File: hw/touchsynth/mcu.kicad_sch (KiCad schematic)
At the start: 10 parts, among them J2 SWIO, J3 MIDI IN, U3 CH32V003F4P6 / CH32V002F4P6, U4 LTV-817S

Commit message: Schematic v2: hand-drawn sheet layouts with wires; MIDI in DNP
- draw.py/gen_sch2.py/layouts.py: placement + wiring per block, automatic
  labels for remaining split nets, short detection, junctions, KiCad
  endpoint-only connection semantics
- all 7 sheets laid out (ladder drawn as a transistor stack, diff amps,
  integrator with reset, R-2R DAC, ...); ERC 0 violations, netlist == design,
  145 simulated elements match
- MIDI input parts marked DNP (footprints kept)
- docs/touchsynth_schematic.pdf

Co-Authored-By: Claude Opus 5.5 (1M context) <noreply@anthropic.com>
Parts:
- D2, R14, R15, U4: now not fitted
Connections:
- net MIDI_4: no longer names the net of J3.1 (Pin_1), R14.1
- net MIDI_5: no longer names the net of D2.2 (A), J3.2 (Pin_2), U4.2
- net MIDI_A: no longer names the net of D2.1 (K), R14.2, U4.1
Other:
- note added: "MCU: CH32V003F4P6 or CH32V002F4P6 (TSSOP-20, hand-soldered, not placed by JLCPCB)"
- note added: "MIDI in (not populated in rev 0.1)"
- note added: "Programming (WCH-LinkE, SWIO)"
- note removed: "MCU (CH32V003 / CH32V002, hand-soldered)"
- note removed: "MIDI in"
- note removed: "Programming (WCH-LinkE)"

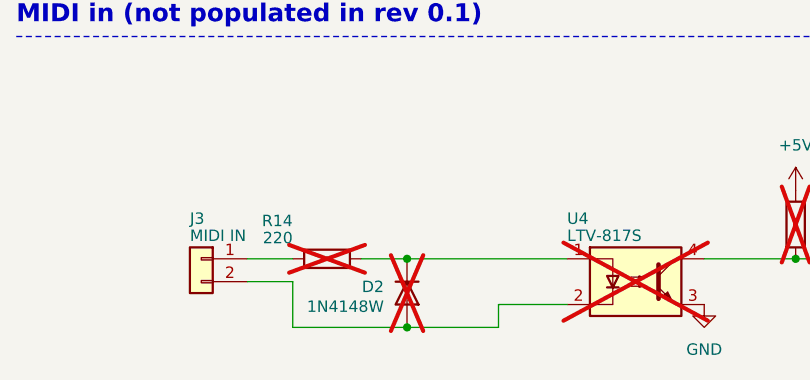
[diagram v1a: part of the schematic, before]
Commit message: PCB placement by functional block, silkscreen art, discrete LED resistors
- gen_pcb.py / pcb_place.py: 100 x 100 mm 2-layer board; keys, LEDs, connectors and test points fixed,
  ICs anchored per block, remaining parts placed greedily by connectivity inside their block
- blocks tile the circuit area with a 0.35 mm street for the dashed silkscreen frames and a reserved
  title tab each (pcb_art.py); piano keybed with hatched black keys; logo, resonant saw and ladder
  response curves on the front; signal-flow diagram on the back
- LED resistor arrays replaced by 16 discrete 4.7k 0603 (basic part) next to each LED
- deterministic schematic UUIDs, net name labels for PCB parity, op-amp re-pairing, fab.py

Co-Authored-By: Claude Opus 5.5 (1M context) <noreply@anthropic.com>
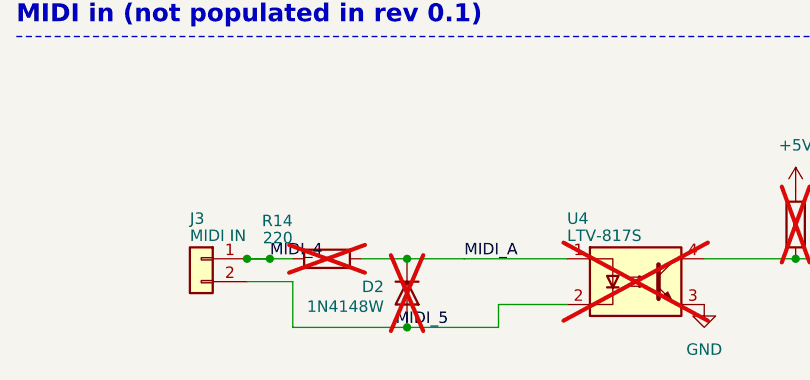
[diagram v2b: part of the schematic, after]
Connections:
- net MIDI_4: now reaches J3.1 (Pin_1), R14.1
- net MIDI_5: now reaches D2.2 (A), J3.2 (Pin_2), U4.2
- net MIDI_A: now reaches D2.1 (K), R14.2, U4.1
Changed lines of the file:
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@@
 	(title_block
 		(title "TouchSynth — MCU, programming header and MIDI in")
-		(date "2026-09-26")
+		(date "2026-09-27")
 		(rev "0.1")
 		(comment 1 "Generated by hw/gen_sch2.py (layouts.py) from hw/design.py")
@@
 		(instances
 			(project "touchsynth"
-				(path "/86f4d9ff-f6c4-486e-8b1b-1bc40a4be669/1b45b040-86f0-443c-a8b0-2b3b25d1fe2a"
+				(path "/c42cd0d4-93b1-5178-97ee-fdd3025be2c6/459cd1ac-5cc8-57d9-a087-d7ee7e1fbcf4"
 					(reference "U3")
 					(unit 1)
@@
 		(instances
 			(project "touchsynth"
-				(path "/86f4d9ff-f6c4-486e-8b1b-1bc40a4be669/1b45b040-86f0-443c-a8b0-2b3b25d1fe2a"
+				(path "/c42cd0d4-93b1-5178-97ee-fdd3025be2c6/459cd1ac-5cc8-57d9-a087-d7ee7e1fbcf4"
 					(reference "J2")
 					(unit 1)
@@
 		(instances
 			(project "touchsynth"
-				(path "/86f4d9ff-f6c4-486e-8b1b-1bc40a4be669/1b45b040-86f0-443c-a8b0-2b3b25d1fe2a"
+				(path "/c42cd0d4-93b1-5178-97ee-fdd3025be2c6/459cd1ac-5cc8-57d9-a087-d7ee7e1fbcf4"
 					(reference "C15")
 					(unit 1)
@@
 		(instances
 			(project "touchsynth"
-				(path "/86f4d9ff-f6c4-486e-8b1b-1bc40a4be669/1b45b040-86f0-443c-a8b0-2b3b25d1fe2a"
+				(path "/c42cd0d4-93b1-5178-97ee-fdd3025be2c6/459cd1ac-5cc8-57d9-a087-d7ee7e1fbcf4"
 					(reference "C16")
 					(unit 1)
@@
 		(instances
 			(project "touchsynth"
-				(path "/86f4d9ff-f6c4-486e-8b1b-1bc40a4be669/1b45b040-86f0-443c-a8b0-2b3b25d1fe2a"
+				(path "/c42cd0d4-93b1-5178-97ee-fdd3025be2c6/459cd1ac-5cc8-57d9-a087-d7ee7e1fbcf4"
 					(reference "J3")
 					(unit 1)
@@
 		(instances
 			(project "touchsynth"
-				(path "/86f4d9ff-f6c4-486e-8b1b-1bc40a4be669/1b45b040-86f0-443c-a8b0-2b3b25d1fe2a"
+				(path "/c42cd0d4-93b1-5178-97ee-fdd3025be2c6/459cd1ac-5cc8-57d9-a087-d7ee7e1fbcf4"
 					(reference "R14")
 					(unit 1)
@@
 		(instances
 			(project "touchsynth"
-				(path "/86f4d9ff-f6c4-486e-8b1b-1bc40a4be669/1b45b040-86f0-443c-a8b0-2b3b25d1fe2a"
+				(path "/c42cd0d4-93b1-5178-97ee-fdd3025be2c6/459cd1ac-5cc8-57d9-a087-d7ee7e1fbcf4"
 					(reference "U4")
 					(unit 1)
@@
 		(instances
 			(project "touchsynth"
-				(path "/86f4d9ff-f6c4-486e-8b1b-1bc40a4be669/1b45b040-86f0-443c-a8b0-2b3b25d1fe2a"
+				(path "/c42cd0d4-93b1-5178-97ee-fdd3025be2c6/459cd1ac-5cc8-57d9-a087-d7ee7e1fbcf4"
 					(reference "D2")
 					(unit 1)
@@
 		(instances
 			(project "touchsynth"
-				(path "/86f4d9ff-f6c4-486e-8b1b-1bc40a4be669/1b45b040-86f0-443c-a8b0-2b3b25d1fe2a"
+				(path "/c42cd0d4-93b1-5178-97ee-fdd3025be2c6/459cd1ac-5cc8-57d9-a087-d7ee7e1fbcf4"
 					(reference "R15")
 					(unit 1)
@@
 		(instances
 			(project "touchsynth"
-				(path "/86f4d9ff-f6c4-486e-8b1b-1bc40a4be669/1b45b040-86f0-443c-a8b0-2b3b25d1fe2a"
+				(path "/c42cd0d4-93b1-5178-97ee-fdd3025be2c6/459cd1ac-5cc8-57d9-a087-d7ee7e1fbcf4"
 					(reference "TP10")
 					(unit 1)
@@
 		(pts
 			(xy 40.64 215.9)
+			(xy 43.18 215.9)
+		)
+		(stroke
+			(width 0)
+			(type default)
+		)
+	)
+	(wire
+		(pts
+			(xy 43.18 215.9)
 			(xy 45.72 215.9)
 		)
@@
 		(pts
 			(xy 58.42 215.9)
+			(xy 64.77 215.9)
+		)
+		(stroke
+			(width 0)
+			(type default)
+		)
+	)
+	(wire
+		(pts
+			(xy 64.77 215.9)
 			(xy 76.2 215.9)
 		)
@@
 		(pts
 			(xy 45.72 223.52)
+			(xy 57.15 223.52)
+		)
+		(stroke
+			(width 0)
+			(type default)
+		)
+	)
+	(wire
+		(pts
+			(xy 57.15 223.52)
 			(xy 58.42 223.52)
 		)
@@
 			(xy 111.76 96.52)
 			(xy 114.3 96.52)
+		)
+		(stroke
+			(width 0)
+			(type default)
+		)
+	)
+	(wire
+		(pts
+			(xy 40.64 215.9)
+			(xy 43.18 215.9)
 		)
 		(stroke
@@
 				(hide yes)
 			)
+		)
+	)
+	(label "MIDI_4"
+		(at 43.18 215.9 0)
+		(effects
+			(font
+				(size 1.27 1.27)
+			)
+			(justify left bottom)
+		)
+	)
+	(label "MIDI_5"
+		(at 57.15 223.52 0)
+		(effects
+			(font
+				(size 1.27 1.27)
+			)
+			(justify left bottom)
+		)
+	)
+	(label "MIDI_A"
+		(at 64.77 215.9 0)
+		(effects
+			(font
+				(size 1.27 1.27)
+			)
+			(justify left bottom)
 		)
 	)
@@
 		(instances
 			(project "touchsynth"
-				(path "/86f4d9ff-f6c4-486e-8b1b-1bc40a4be669/1b45b040-86f0-443c-a8b0-2b3b25d1fe2a"
+				(path "/c42cd0d4-93b1-5178-97ee-fdd3025be2c6/459cd1ac-5cc8-57d9-a087-d7ee7e1fbcf4"
 					(reference "#PWR02001")
 					(unit 1)
@@
 		(instances
 			(project "touchsynth"
-				(path "/86f4d9ff-f6c4-486e-8b1b-1bc40a4be669/1b45b040-86f0-443c-a8b0-2b3b25d1fe2a"
+				(path "/c42cd0d4-93b1-5178-97ee-fdd3025be2c6/459cd1ac-5cc8-57d9-a087-d7ee7e1fbcf4"
 					(reference "#PWR02002")
 					(unit 1)
@@
 		(instances
 			(project "touchsynth"
-				(path "/86f4d9ff-f6c4-486e-8b1b-1bc40a4be669/1b45b040-86f0-443c-a8b0-2b3b25d1fe2a"
+				(path "/c42cd0d4-93b1-5178-97ee-fdd3025be2c6/459cd1ac-5cc8-57d9-a087-d7ee7e1fbcf4"
 					(reference "#PWR02003")
 					(unit 1)
@@
 		(instances
 			(project "touchsynth"
-				(path "/86f4d9ff-f6c4-486e-8b1b-1bc40a4be669/1b45b040-86f0-443c-a8b0-2b3b25d1fe2a"
+				(path "/c42cd0d4-93b1-5178-97ee-fdd3025be2c6/459cd1ac-5cc8-57d9-a087-d7ee7e1fbcf4"
 					(reference "#PWR02004")
 					(unit 1)
@@
 		(instances
 			(project "touchsynth"
-				(path "/86f4d9ff-f6c4-486e-8b1b-1bc40a4be669/1b45b040-86f0-443c-a8b0-2b3b25d1fe2a"
+				(path "/c42cd0d4-93b1-5178-97ee-fdd3025be2c6/459cd1ac-5cc8-57d9-a087-d7ee7e1fbcf4"
 					(reference "#PWR02005")
 					(unit 1)
@@
 		(instances
 			(project "touchsynth"
-				(path "/86f4d9ff-f6c4-486e-8b1b-1bc40a4be669/1b45b040-86f0-443c-a8b0-2b3b25d1fe2a"
+				(path "/c42cd0d4-93b1-5178-97ee-fdd3025be2c6/459cd1ac-5cc8-57d9-a087-d7ee7e1fbcf4"
 					(reference "#PWR02006")
 					(unit 1)
@@
 		(instances
 			(project "touchsynth"
-				(path "/86f4d9ff-f6c4-486e-8b1b-1bc40a4be669/1b45b040-86f0-443c-a8b0-2b3b25d1fe2a"
+				(path "/c42cd0d4-93b1-5178-97ee-fdd3025be2c6/459cd1ac-5cc8-57d9-a087-d7ee7e1fbcf4"
 					(reference "#PWR02007")
 					(unit 1)
@@
 		(instances
 			(project "touchsynth"
-				(path "/86f4d9ff-f6c4-486e-8b1b-1bc40a4be669/1b45b040-86f0-443c-a8b0-2b3b25d1fe2a"
+				(path "/c42cd0d4-93b1-5178-97ee-fdd3025be2c6/459cd1ac-5cc8-57d9-a087-d7ee7e1fbcf4"
 					(reference "#PWR02008")
 					(unit 1)
@@
 		(instances
 			(project "touchsynth"
-				(path "/86f4d9ff-f6c4-486e-8b1b-1bc40a4be669/1b45b040-86f0-443c-a8b0-2b3b25d1fe2a"
+				(path "/c42cd0d4-93b1-5178-97ee-fdd3025be2c6/459cd1ac-5cc8-57d9-a087-d7ee7e1fbcf4"
 					(reference "#PWR02009")
 					(unit 1)
@@
 		(instances
 			(project "touchsynth"
-				(path "/86f4d9ff-f6c4-486e-8b1b-1bc40a4be669/1b45b040-86f0-443c-a8b0-2b3b25d1fe2a"
+				(path "/c42cd0d4-93b1-5178-97ee-fdd3025be2c6/459cd1ac-5cc8-57d9-a087-d7ee7e1fbcf4"
 					(reference "#PWR02010")
 					(unit 1)
@@
 	)
 	(junction
+		(at 40.64 215.9)
+		(diameter 0)
+		(color 0 0 0 0)
+	)
+	(junction
+		(at 43.18 215.9)
+		(diameter 0)
+		(color 0 0 0 0)
+	)
+	(junction

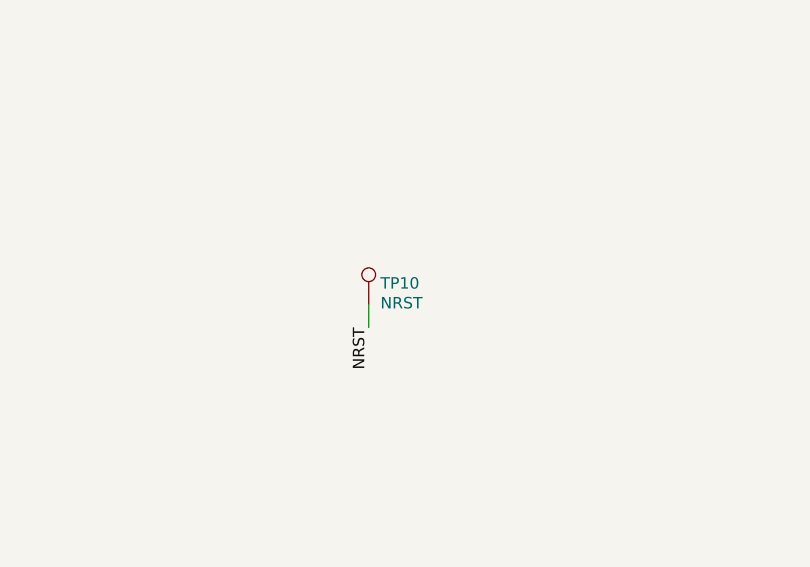
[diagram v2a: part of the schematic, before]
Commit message: 4-layer PCB: keys I/O row, trim DAC by the VCA, full routing and fab outputs
- 4 layers: F.Cu signals, In1 solid GND, In2 split power (VP analog / +5V digital / GND under the keys),
  B.Cu signals; no plane and no foreign tracks under the touch pads
- floorplan: analog blocks 72 x 36 mm in signal-flow order, right column MIDI / trim DAC / MCU,
  keys I/O row (touch muxes, LED shift registers) directly above the keys; shorter white keys,
  function pads flush with the keybed; test points inside their blocks, two THT scope-ground pins
- routing pipeline: plane stitch vias, pre-routed plane nets, Freerouting, GND via grid, island
  check, A* maze router for leftovers (pcb_maze.py), rip-up repair mode
- DRC: 0 violations, 0 unconnected, schematic parity OK; JLCPCB gerbers / BOM / CPL via fab.py
- silkscreen: back-side credits (design: cpldcpu & Claude Opus 5.5), vias kept out of the art

Co-Authored-By: Claude Opus 5.5 (1M context) <noreply@anthropic.com>
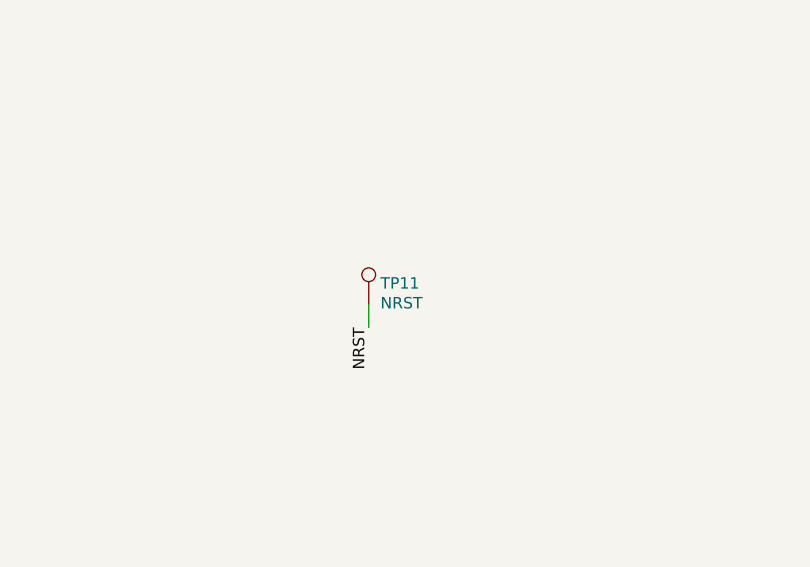
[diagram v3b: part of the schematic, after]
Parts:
- removed TP10: NRST, TestPoint:TestPoint_Pad_D1.0mm, symbol Connector:TestPoint
- added TP11: NRST, TestPoint:TestPoint_Pad_D1.0mm, symbol Connector:TestPoint
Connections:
- net NRST: now also TP11.1
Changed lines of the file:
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@@
 		(on_board yes)
 		(dnp no)
-		(property "Reference" "TP10"
+		(property "Reference" "TP11"
 			(at 301.02 99.249 0)
 			(effects
@@
 			(project "touchsynth"
 				(path "/c42cd0d4-93b1-5178-97ee-fdd3025be2c6/459cd1ac-5cc8-57d9-a087-d7ee7e1fbcf4"
-					(reference "TP10")
+					(reference "TP11")
 					(unit 1)
 				)
